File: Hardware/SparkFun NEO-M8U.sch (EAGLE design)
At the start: 50 parts, among them J13 U.FL, J2 Qwiic Right Angle, J4 Qwiic Right Angle, U2 3.3V

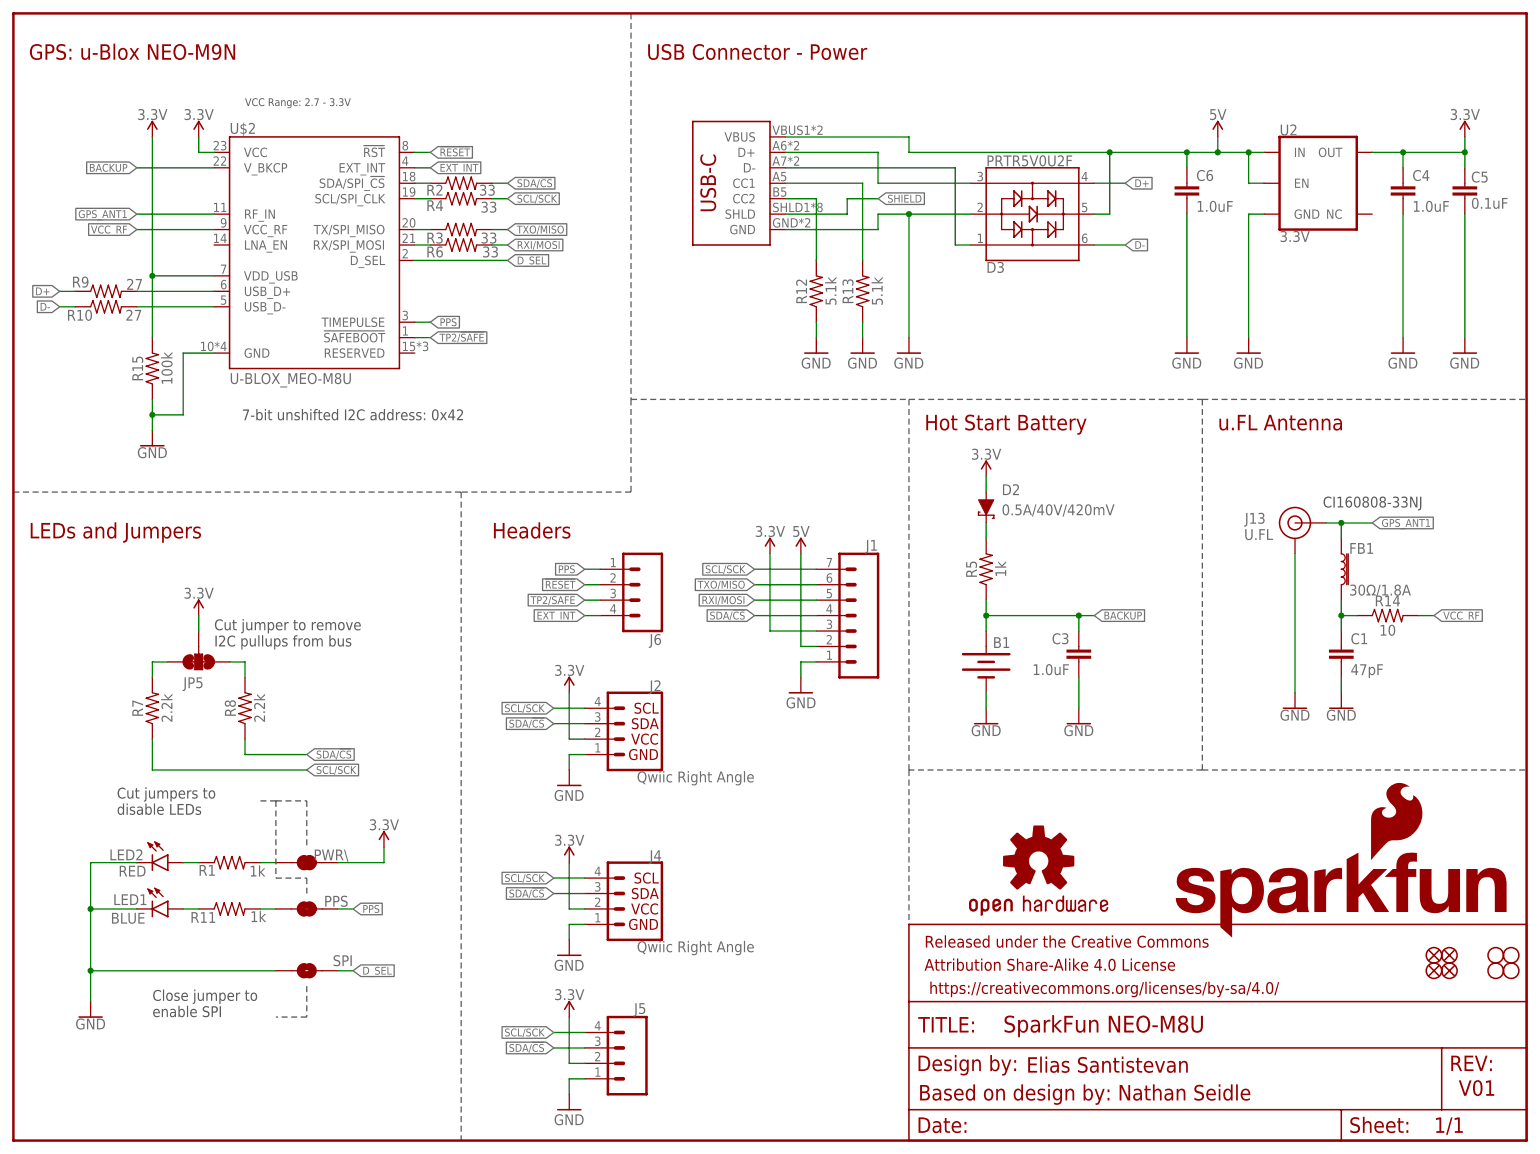
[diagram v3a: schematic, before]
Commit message: Updates old schematic artifacts, replace power lables with their proper symbols
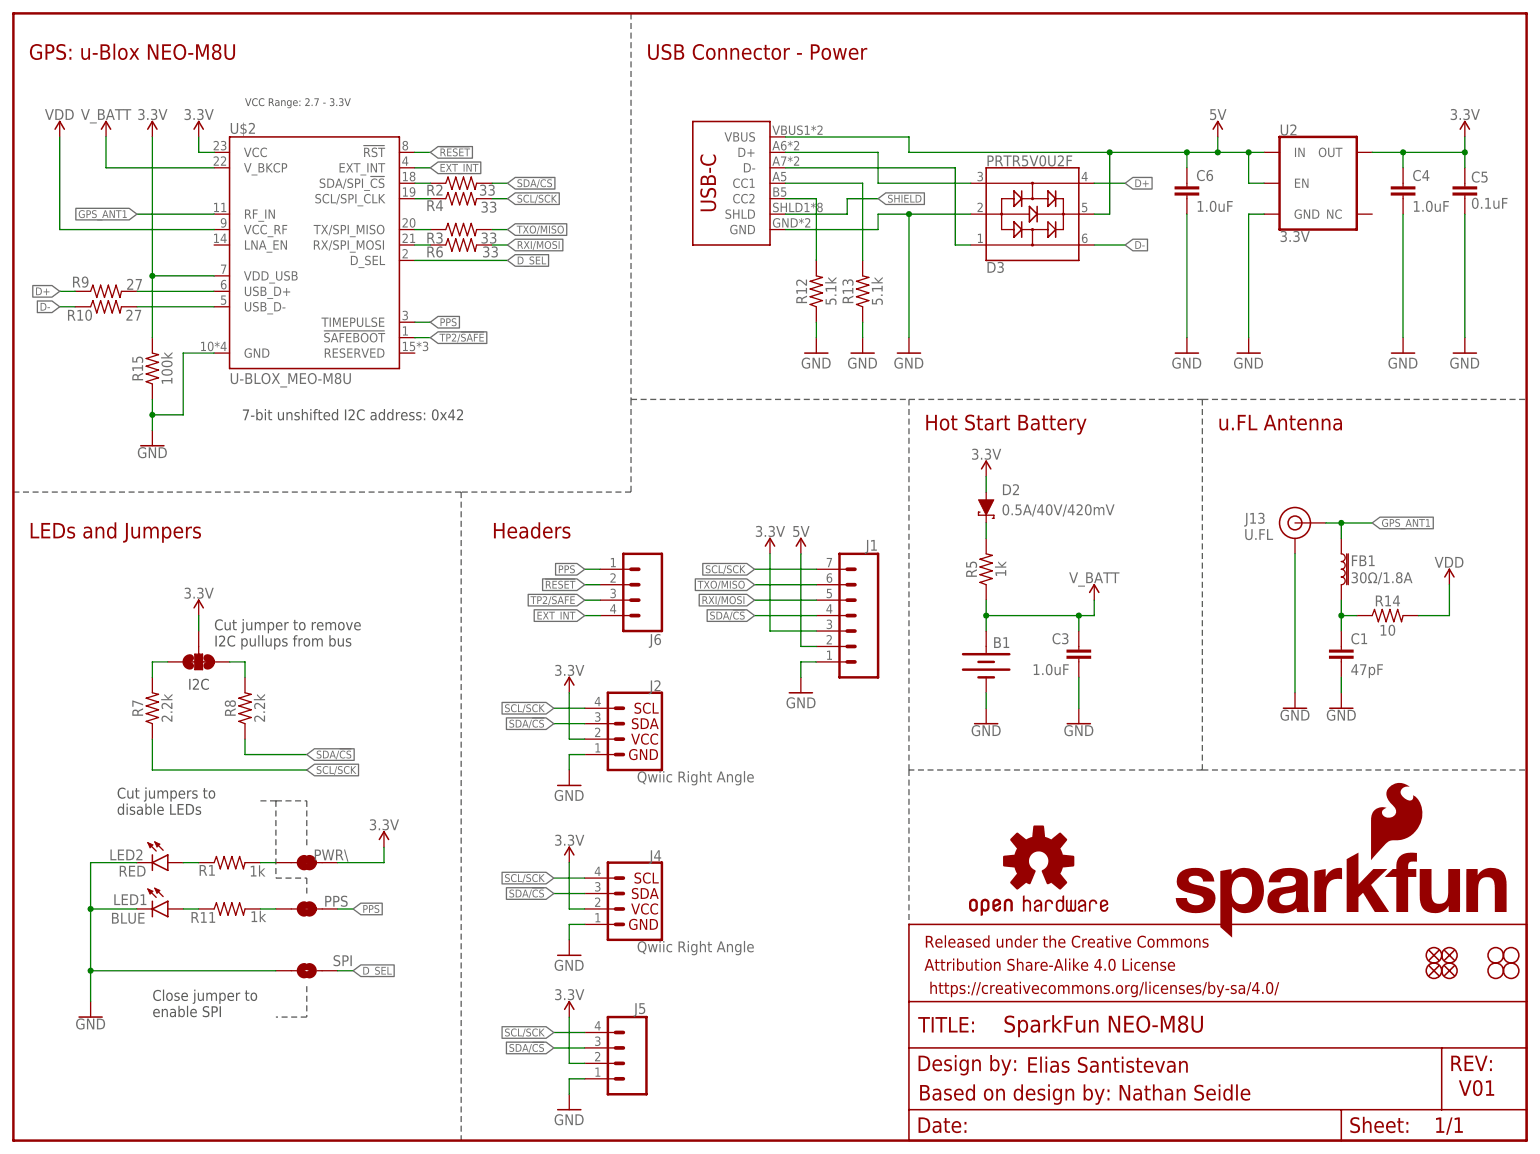
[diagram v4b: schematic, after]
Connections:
- net BACKUP renamed V_BATT
- net VCC_RF renamed VDD
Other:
- note added: "GPS: u-Blox NEO-M8U"
- note added: "I2C"
- note removed: "CI160808-33NJ"
- note removed: "GPS: u-Blox NEO-M9N"
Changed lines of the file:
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@@
 <part name="J6" library="SparkFun-Connectors" deviceset="CONN_04" device="1X04_NO_SILK"/>
 <part name="U$2" library="SparkFun-GPS" deviceset="U-BLOX_MEO-M8U" device=""/>
+<part name="SUPPLY12" library="SparkFun-PowerSymbols" deviceset="V_BATT" device=""/>
+<part name="SUPPLY13" library="SparkFun-PowerSymbols" deviceset="V_BATT" device=""/>
+<part name="SUPPLY14" library="SparkFun-PowerSymbols" deviceset="VDD" device=""/>
+<part name="SUPPLY15" library="SparkFun-PowerSymbols" deviceset="VDD" device=""/>
 </parts>
 <sheets>
@@
 <text x="22.86" y="20.32" size="1.778" layer="97" font="vector">Close jumper to
 enable SPI</text>
-<text x="215.392" y="104.14" size="1.778" layer="97" font="vector">CI160808-33NJ</text>
 <text x="166.624" y="11.176" size="2.54" layer="94" font="vector">Elias Santistevan</text>
 <text x="78.74" y="99.06" size="2.54" layer="94" font="vector">Headers</text>
 <text x="2.54" y="99.06" size="2.54" layer="94" font="vector">LEDs and Jumpers</text>
 <text x="149.86" y="116.84" size="2.54" layer="94" font="vector">Hot Start Battery</text>
-<text x="2.54" y="177.8" size="2.54" layer="94" font="vector">GPS: u-Blox NEO-M9N </text>
+<text x="2.54" y="177.8" size="2.54" layer="94" font="vector">GPS: u-Blox NEO-M8U</text>
 <wire x1="73.66" y1="106.68" x2="73.66" y2="0" width="0.1524" layer="97" style="shortdash"/>
 <wire x1="40.64" y1="55.88" x2="43.18" y2="55.88" width="0.2032" layer="97" style="dashdot"/>
@@
 <wire x1="43.18" y1="43.18" x2="48.26" y2="43.18" width="0.2032" layer="97" style="dashdot"/>
 <wire x1="48.26" y1="43.18" x2="48.26" y2="40.64" width="0.2032" layer="97" style="dashdot"/>
+<text x="28.702" y="74.168" size="1.778" layer="97" font="vector">I2C</text>
 </plain>
 <instances>
@@
 <attribute name="VALUE" x="39.624" y="71.12" size="1.778" layer="96" font="vector" rot="R90" align="top-center"/>
 </instance>
-<instance part="JP5" gate="G$1" x="30.48" y="78.74" smashed="yes" rot="R270">
-<attribute name="NAME" x="27.94" y="74.422" size="1.778" layer="95" font="vector"/>
-</instance>
+<instance part="JP5" gate="G$1" x="30.48" y="78.74" smashed="yes" rot="R270"/>
 <instance part="SUPPLY9" gate="G$1" x="30.48" y="86.36" smashed="yes">
 <attribute name="VALUE" x="30.48" y="89.154" size="1.778" layer="96" font="vector" align="bottom-center"/>
@@
 </instance>
 <instance part="FB1" gate="G$1" x="218.44" y="93.98" smashed="yes">
-<attribute name="NAME" x="219.71" y="96.52" size="1.778" layer="95" font="vector"/>
-<attribute name="VALUE" x="219.71" y="91.44" size="1.778" layer="96" font="vector" align="top-left"/>
+<attribute name="NAME" x="219.964" y="94.488" size="1.778" layer="95" font="vector"/>
+<attribute name="VALUE" x="219.964" y="93.472" size="1.778" layer="96" font="vector" align="top-left"/>
 </instance>
 <instance part="SUPPLY10" gate="G$1" x="124.46" y="96.52" smashed="yes">
@@
 <attribute name="NAME" x="35.56" y="165.608" size="1.778" layer="95"/>
 <attribute name="VALUE" x="35.56" y="124.46" size="1.778" layer="96"/>
+</instance>
+<instance part="SUPPLY12" gate="G$1" x="177.8" y="88.9" smashed="yes">
+<attribute name="VALUE" x="177.8" y="91.694" size="1.778" layer="96" align="bottom-center"/>
+</instance>
+<instance part="SUPPLY13" gate="G$1" x="15.24" y="165.1" smashed="yes">
+<attribute name="VALUE" x="15.24" y="167.894" size="1.778" layer="96" align="bottom-center"/>
+</instance>
+<instance part="SUPPLY14" gate="VDD" x="7.62" y="165.1" smashed="yes">
+<attribute name="VALUE" x="7.62" y="167.894" size="1.778" layer="96" align="bottom-center"/>
+</instance>
+<instance part="SUPPLY15" gate="VDD" x="236.22" y="91.44" smashed="yes">
+<attribute name="VALUE" x="236.22" y="94.234" size="1.778" layer="96" align="bottom-center"/>
 </instance>
 </instances>
@@
 <label x="93.98" y="93.98" size="1.27" layer="95" font="vector" rot="MR0" xref="yes"/>
 <pinref part="J6" gate="J1" pin="1"/>
-</segment>
-</net>
-<net name="BACKUP" class="0">
-<segment>
-<pinref part="C3" gate="G$1" pin="1"/>
-<wire x1="175.26" y1="86.36" x2="175.26" y2="83.82" width="0.1524" layer="91"/>
-<pinref part="B1" gate="G$1" pin="+"/>
-<wire x1="175.26" y1="86.36" x2="160.02" y2="86.36" width="0.1524" layer="91"/>
-<wire x1="160.02" y1="86.36" x2="160.02" y2="83.82" width="0.1524" layer="91"/>
-<wire x1="175.26" y1="86.36" x2="177.8" y2="86.36" width="0.1524" layer="91"/>
-<junction x="175.26" y="86.36"/>
-<label x="177.8" y="86.36" size="1.27" layer="95" font="vector" xref="yes"/>
-<pinref part="R5" gate="G$1" pin="1"/>
-<wire x1="160.02" y1="88.9" x2="160.02" y2="86.36" width="0.1524" layer="91"/>
-<junction x="160.02" y="86.36"/>
-</segment>
-<segment>
-<wire x1="33.02" y1="160.02" x2="20.32" y2="160.02" width="0.1524" layer="91"/>
-<label x="20.32" y="160.02" size="1.27" layer="95" font="vector" rot="R180" xref="yes"/>
-<pinref part="U$2" gate="G$1" pin="V_BKCP"/>
 </segment>
 </net>
@@
 </segment>
 </net>
-<net name="VCC_RF" class="0">
-<segment>
-<wire x1="33.02" y1="149.86" x2="20.32" y2="149.86" width="0.1524" layer="91"/>
-<label x="20.32" y="149.86" size="1.27" layer="95" rot="R180" xref="yes"/>
-<pinref part="U$2" gate="G$1" pin="VCC_RF"/>
-</segment>
-<segment>
-<pinref part="R14" gate="G$1" pin="2"/>
-<wire x1="233.68" y1="86.36" x2="231.14" y2="86.36" width="0.1524" layer="91"/>
-<label x="233.68" y="86.36" size="1.27" layer="95" xref="yes"/>
-</segment>
-</net>
 <net name="ANT_VCC" class="0">
 <segment>
@@
 </segment>
 </net>
+<net name="V_BATT" class="0">
+<segment>
+<pinref part="SUPPLY13" gate="G$1" pin="V_BATT"/>
+<wire x1="15.24" y1="165.1" x2="15.24" y2="160.02" width="0.1524" layer="91"/>
+<wire x1="33.02" y1="160.02" x2="15.24" y2="160.02" width="0.1524" layer="91"/>
+<pinref part="U$2" gate="G$1" pin="V_BKCP"/>
+</segment>
+<segment>
+<pinref part="C3" gate="G$1" pin="1"/>
+<wire x1="175.26" y1="86.36" x2="175.26" y2="83.82" width="0.1524" layer="91"/>
+<pinref part="B1" gate="G$1" pin="+"/>
+<wire x1="175.26" y1="86.36" x2="160.02" y2="86.36" width="0.1524" layer="91"/>
+<wire x1="160.02" y1="86.36" x2="160.02" y2="83.82" width="0.1524" layer="91"/>
+<junction x="175.26" y="86.36"/>
+<pinref part="R5" gate="G$1" pin="1"/>
+<wire x1="160.02" y1="88.9" x2="160.02" y2="86.36" width="0.1524" layer="91"/>
+<junction x="160.02" y="86.36"/>
+<pinref part="SUPPLY12" gate="G$1" pin="V_BATT"/>
+<wire x1="177.8" y1="88.9" x2="177.8" y2="86.36" width="0.1524" layer="91"/>
+<wire x1="177.8" y1="86.36" x2="175.26" y2="86.36" width="0.1524" layer="91"/>
+</segment>
+</net>
+<net name="VDD" class="0">
+<segment>
+<pinref part="U$2" gate="G$1" pin="VCC_RF"/>
+<wire x1="33.02" y1="149.86" x2="7.62" y2="149.86" width="0.1524" layer="91"/>
+<pinref part="SUPPLY14" gate="VDD" pin="VDD"/>
+<wire x1="7.62" y1="149.86" x2="7.62" y2="165.1" width="0.1524" layer="91"/>
+</segment>
+<segment>
+<pinref part="R14" gate="G$1" pin="2"/>
+<wire x1="231.14" y1="86.36" x2="236.22" y2="86.36" width="0.1524" layer="91"/>
+<pinref part="SUPPLY15" gate="VDD" pin="VDD"/>
+<wire x1="236.22" y1="86.36" x2="236.22" y2="91.44" width="0.1524" layer="91"/>
+</segment>
+</net>

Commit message: Rolls version to v10 and updates all of the parts' packages
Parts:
- J3: device SparkFun-Connectors:USB_C2-LAYER -> SparkFun-Connectors:USB_C_2-LAYER_PADS
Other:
- note added: "V10"
- note removed: "V01"
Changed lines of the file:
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@@
 <?xml version="1.0" encoding="utf-8"?>
 <!DOCTYPE eagle SYSTEM "eagle.dtd">
-<eagle version="9.5.1">
+<eagle version="9.5.2">
 <drawing>
 <settings>
@@
 <part name="D3" library="SparkFun-IC-Power" deviceset="PRTR5V0U2" device="F"/>
 <part name="J5" library="SparkFun-Connectors" deviceset="CONN_04" device="1X04_NO_SILK"/>
-<part name="J3" library="SparkFun-Connectors" deviceset="USB_C" device="2-LAYER"/>
+<part name="J3" library="SparkFun-Connectors" deviceset="USB_C" device="_2-LAYER_PADS"/>
 <part name="R12" library="SparkFun-Resistors" deviceset="5.1KOHM" device="5.1KOHM-0603-1/10W-1%" value="5.1k"/>
 <part name="R13" library="SparkFun-Resistors" deviceset="5.1KOHM" device="5.1KOHM-0603-1/10W-1%" value="5.1k"/>
@@
 <sheet>
 <plain>
-<text x="237.744" y="7.366" size="2.54" layer="94" font="vector">V01</text>
+<text x="237.744" y="7.366" size="2.54" layer="94" font="vector">V10</text>
 <text x="55.88" y="119.38" size="1.778" layer="97" font="vector" align="center">7-bit unshifted I2C address: 0x42</text>
 <wire x1="0" y1="106.68" x2="73.66" y2="106.68" width="0.1524" layer="97" style="shortdash"/>
